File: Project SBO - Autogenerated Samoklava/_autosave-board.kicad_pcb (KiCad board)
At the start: 2 copper layers, 122.3 x 118.1 mm, 44 parts, among them J1 Jumper, J2 Jumper

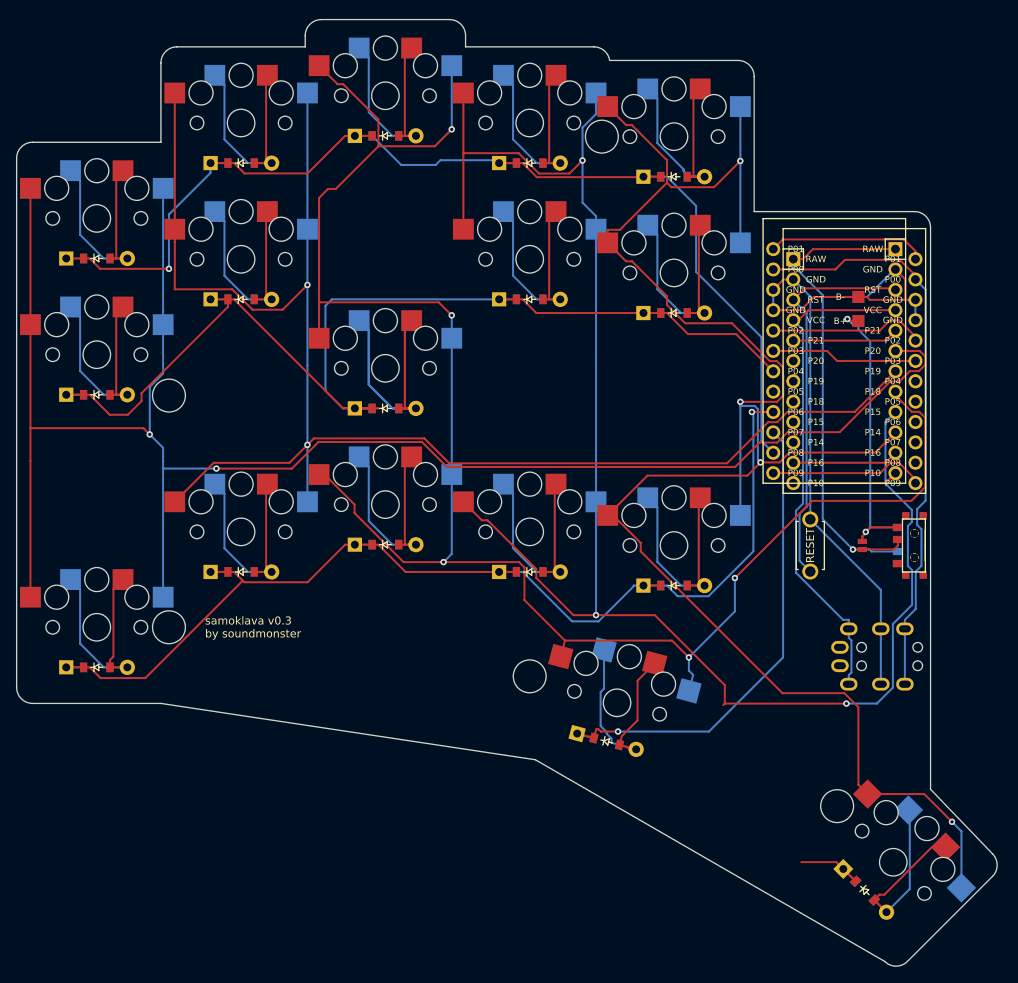
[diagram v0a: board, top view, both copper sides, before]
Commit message: alt finger homing layout
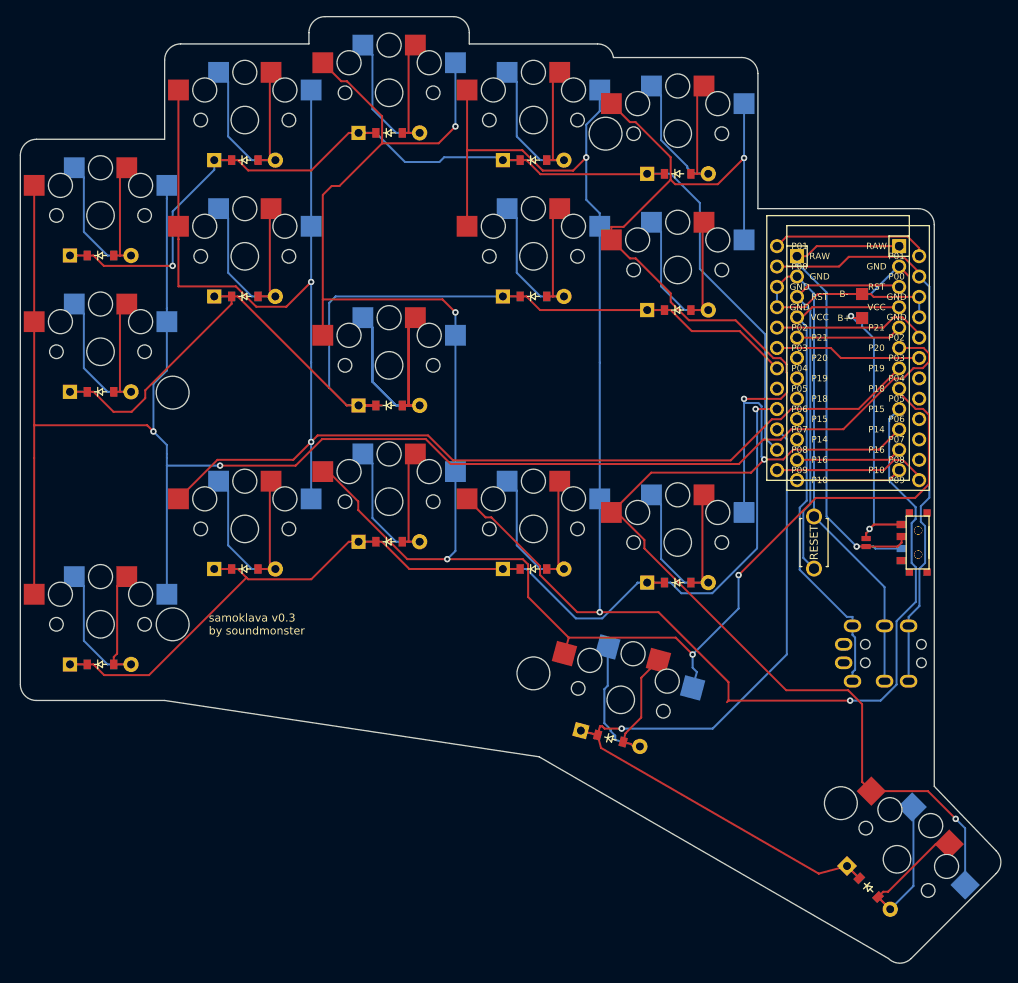
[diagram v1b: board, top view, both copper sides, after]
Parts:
- moved D1 0.59 mm to (0.46, 4.63)
- moved D20 0.59 mm to (72.5, -56.6)
- moved B1 0.59 mm to (89.5, -10.6)
- moved TRRS1 0.59 mm to (104.5, 4.43)
- moved S9 0.59 mm to (36.5, -15.7)
- moved D16 0.59 mm to (54.5, -58.3)
- moved S16 0.59 mm to (54.5, -63.3)
- moved D12 0.59 mm to (36.5, -61.7)
- moved S21 0.59 mm to (65.4, 9.05)
- moved D23 0.59 mm to (96.3, 32.5)
- moved S3 0.59 mm to (0.46, -34.4)
- moved S11 0.59 mm to (36.5, -32.7)
- moved S1 0.59 mm to (0.46, -0.37)
- moved J1 0.59 mm to (96.0, -10.6)
- moved J2 0.59 mm to (96.0, -10.6)
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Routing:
- net row_thumb: track 71.3 -> 102.4 mm
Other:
- outline, holes or cut-outs redrawn
